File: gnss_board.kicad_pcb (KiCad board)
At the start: 4 copper layers, 102.2 x 100.3 mm, 118 parts, among them J1 Conn_01x10_Pin, J2 Serial Connector, J3 U.FL, J4 Conn_01x04_Pin, Q1 BC817, Q2 BC817, T1 LMUN2211LT1G, U1 H1102NL, U2 LAN8710A, U4 TX4138(ESOIC-8)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

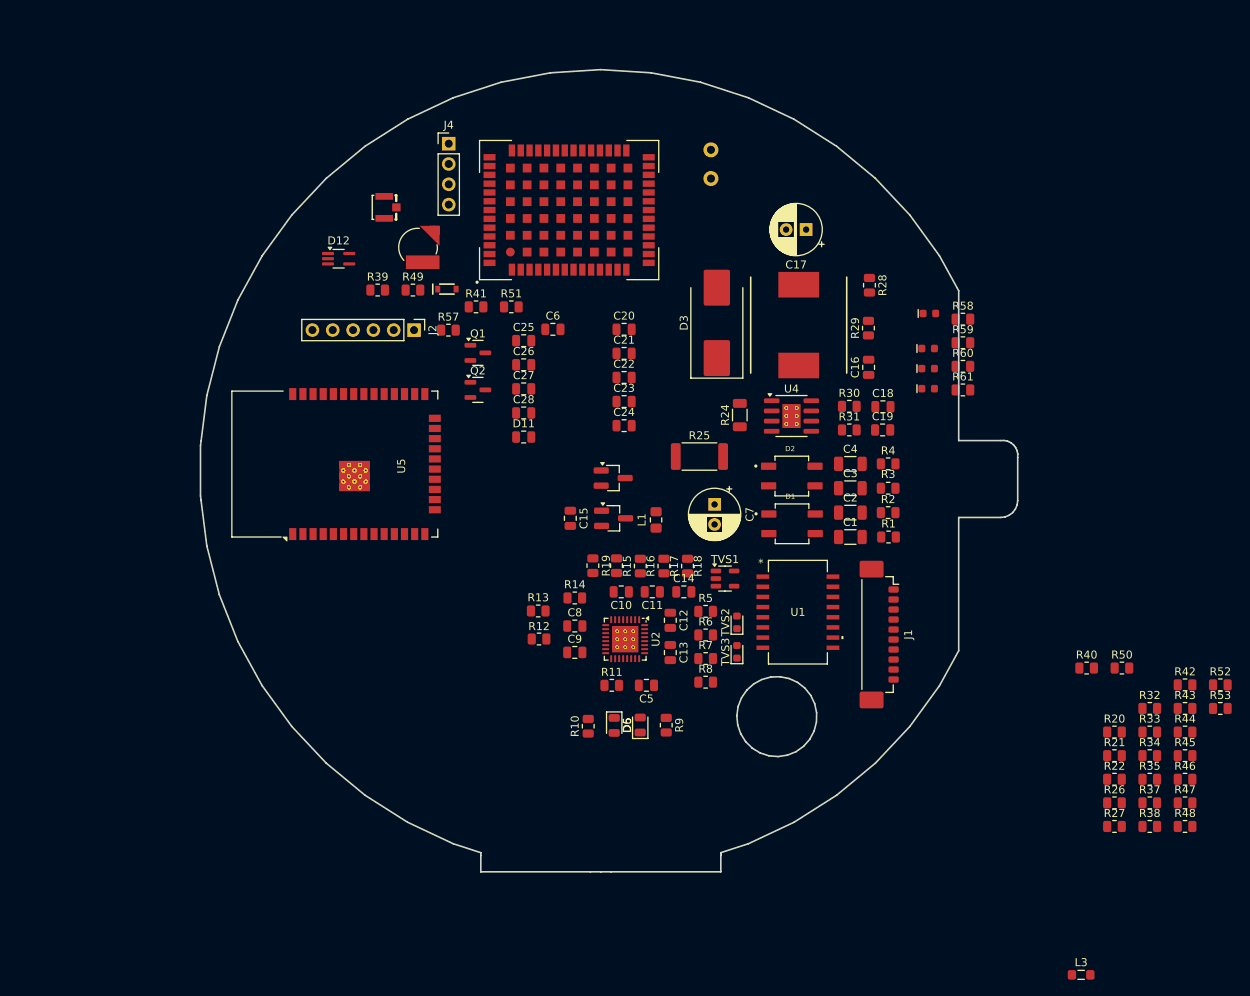
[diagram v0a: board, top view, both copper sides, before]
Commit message: All components have been added
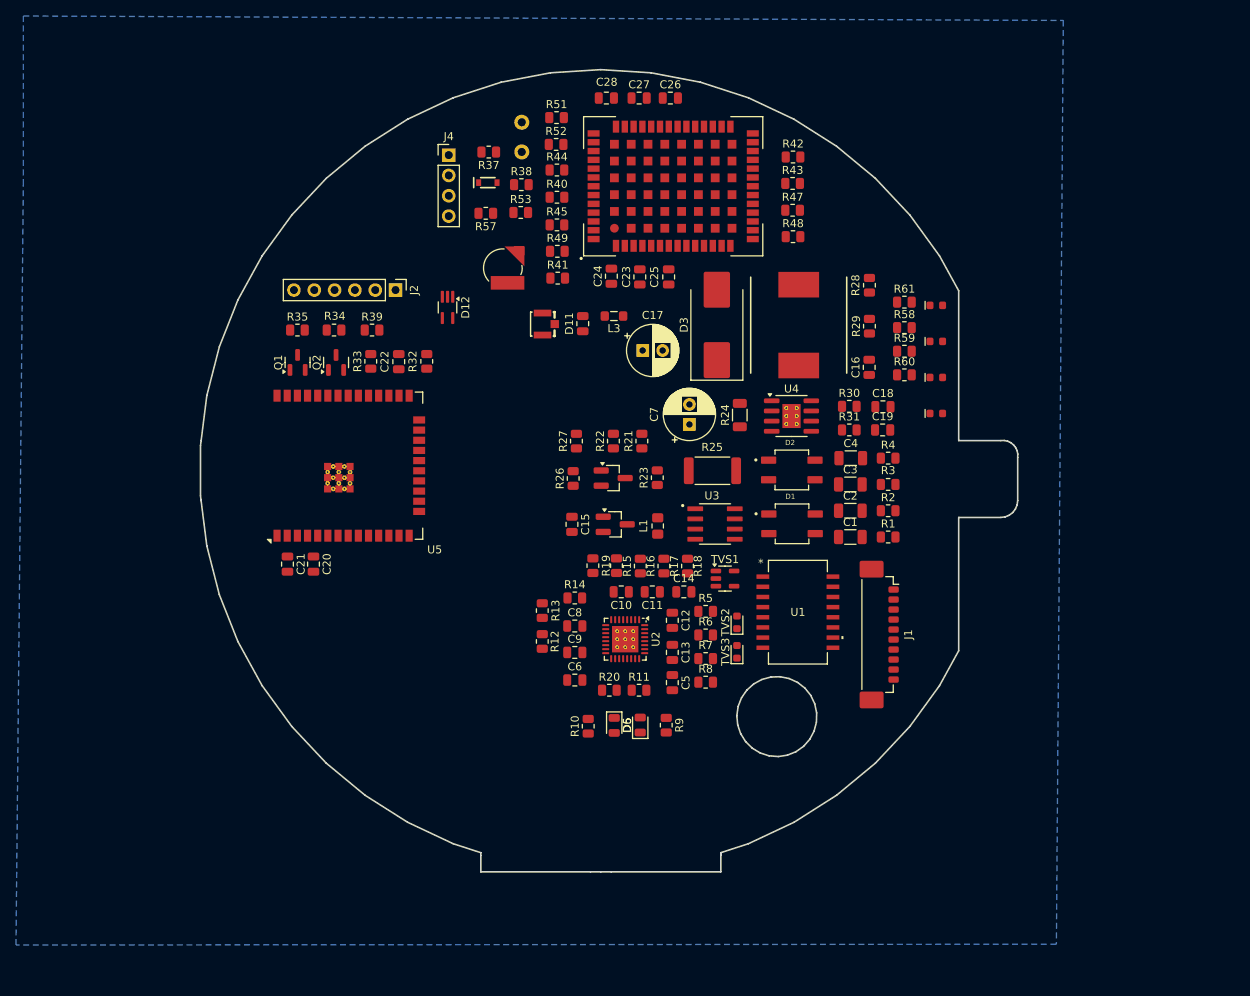
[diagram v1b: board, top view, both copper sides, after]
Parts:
- removed R46, R50: 33R, Resistor_SMD:R_0805_2012Metric
- added R23: 24.9K, Resistor_SMD:R_0805_2012Metric, F.Cu at (102.8, 79.5)
- added U3: TPS2375D, gnss_board:SOIC127P599X175-8N, F.Cu at (110.0, 85.2)
- U5: footprint RF_Module:ESP32-WROOM-32D -> RF_Module:ESP32-WROOM-32E
- moved R35 120.4 mm to (57.8, 61.0)
- moved R37 116.0 mm to (81.8, 38.8), turned to 180 degrees
- moved R34 115.0 mm to (62.4, 61.0), turned to 180 degrees
- moved R38 112.3 mm to (85.8, 42.8)
- moved R33 107.8 mm to (67.0, 64.9), turned to 90 degrees
- moved R53 107.2 mm to (85.8, 46.3)
- moved R52 107.0 mm to (90.2, 37.8)
- moved R44 105.4 mm to (90.3, 41.0)
- moved R45 102.8 mm to (90.3, 47.9)
- moved L3 101.0 mm to (97.4, 59.2), turned to 180 degrees
- moved R32 100.3 mm to (74.0, 64.9), turned to -90 degrees
- moved R47 88.8 mm to (119.7, 46.0)
- moved R40 88.6 mm to (90.3, 44.4)
- moved R48 88.5 mm to (119.8, 49.3)
- moved R27 82.7 mm to (92.7, 74.9), turned to 90 degrees
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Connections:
- U6 pad 21: Net-(U6-ERR_STAT) -> unconnected-(U6-ERR_STAT-Pad21)
- U6 pad 51: Net-(U6-EVENT) -> unconnected-(U6-EVENT-Pad51)
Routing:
- added copper zone on B.Cu, net GND

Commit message: Playing around with the auto-router
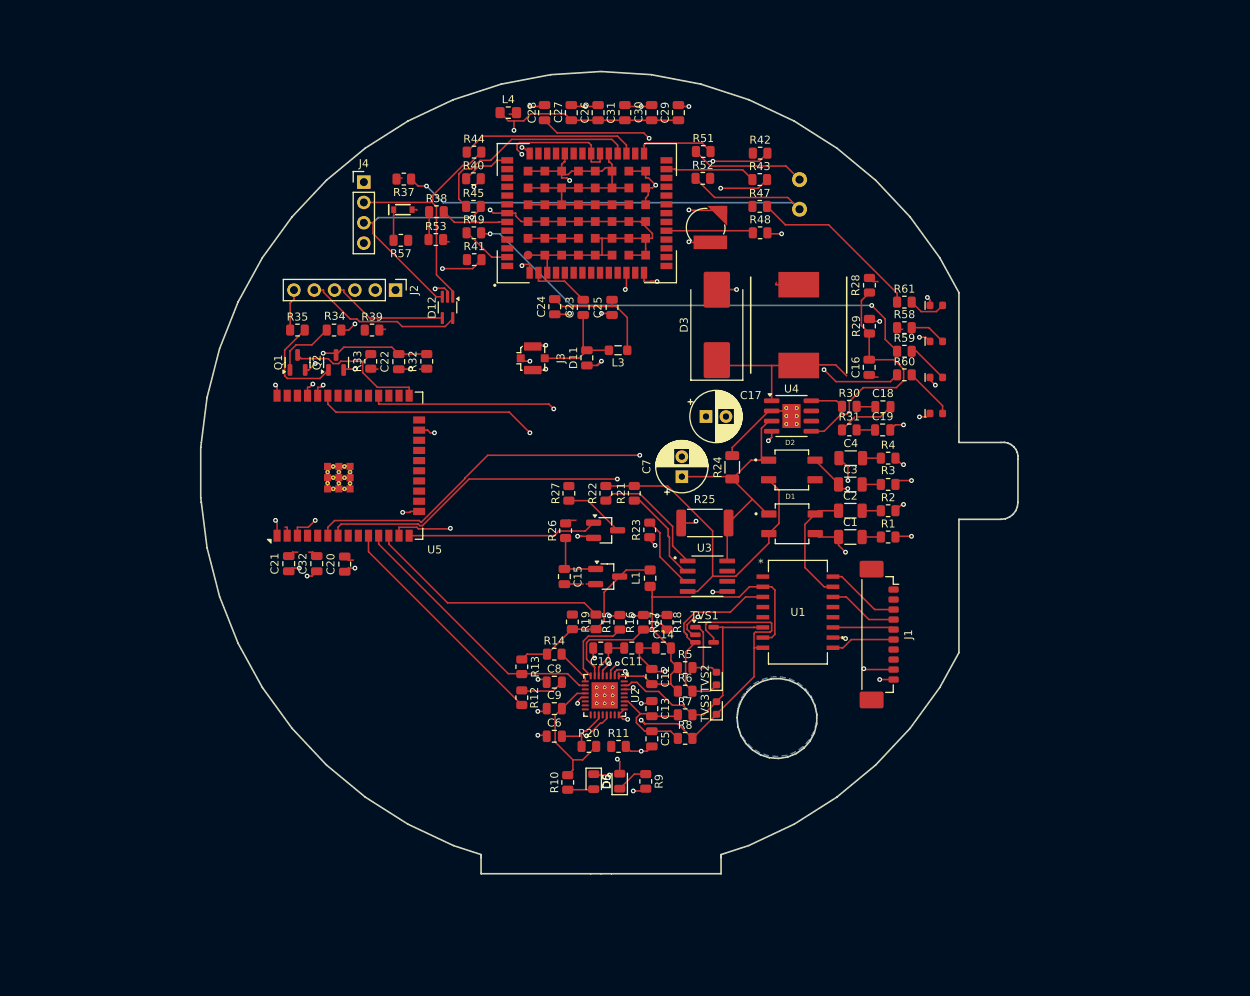
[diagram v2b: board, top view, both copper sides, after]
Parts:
- added C29: 10uF, Capacitor_SMD:C_0805_2012Metric, F.Cu at (105.5, 33.8)
- added C30: 10uF, Capacitor_SMD:C_0805_2012Metric, F.Cu at (102.1, 33.8)
- added C31: 10uF, Capacitor_SMD:C_0805_2012Metric, F.Cu at (98.8, 33.8)
- added C32: 22uF, Capacitor_SMD:C_0805_2012Metric, F.Cu at (60.2, 90.2)
- added L4: FB0805, Inductor_SMD:L_0805_2012Metric_Pad1.15x1.40mm_HandSolder, F.Cu at (84.2, 33.8)
- C26: value 2.2uF -> 10uF
- J3: footprint SparkFun-Connector:U.FL -> Connector_Coaxial:U.FL_Molex_MCRF_73412-0110_Vertical
- moved TP1 35.5 mm to (120.6, 45.9)
- moved TP2 35.5 mm to (120.6, 42.2)
- moved BT1 25.9 mm to (108.9, 48.2)
- moved R51 18.8 mm to (108.6, 38.7)
- moved R52 18.8 mm to (108.5, 42.0)
- moved C17 11.4 mm to (108.9, 71.8)
- moved U6 11.3 mm to (94.0, 46.4)
- moved J4 11.1 mm to (66.1, 42.5)
- moved R37 11.1 mm to (71.1, 42.1)
- moved R38 11.1 mm to (75.2, 46.2)
- moved R53 11.1 mm to (75.1, 49.7)
- moved R57 11.1 mm to (70.8, 49.8)
- moved D10 11.1 mm to (71.0, 45.9)
- moved R40 10.7 mm to (79.8, 42.1)
- moved R41 10.7 mm to (79.9, 52.2)
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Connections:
- net Net-(D3-K) renamed /SW
- C26 pad 2: +3.3V -> VCC
- C27 pad 2: +3.3V -> VCC
- U6 pad 33: +3.3V -> VCC
- U6 pad 34: +3.3V -> VCC
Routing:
- net GND: track 0.00 -> 223.9 mm, vias 0 -> 54
- net GNSS_RXD2: track 0.00 -> 94.8 mm, vias 0 -> 2
- net GNSS_TXD2: track 0.00 -> 91.7 mm, vias 0 -> 2
- net ETH_TX_EN: track 0.00 -> 72.5 mm, vias 0 -> 2
- net Net-(R37-Pad1): track 0.00 -> 64.7 mm, vias 0 -> 1
- net VDD1A: track 0.00 -> 60.3 mm
- net ETH_CLK_IN: track 0.00 -> 59.8 mm, vias 0 -> 2
- net GNSS_PPS: track 0.00 -> 59.6 mm, vias 0 -> 2
- net GNSS_TXD1: track 0.00 -> 53.2 mm, vias 0 -> 2
- net RD-: track 0.00 -> 47.3 mm, vias 0 -> 2
- net +3.3VLAN: track 0.00 -> 45.5 mm
- net VIN+: track 0.00 -> 44.3 mm, vias 0 -> 1
- net VCC: track 0.00 -> 43.2 mm, vias 0 -> 2
- net VIN-: track 0.00 -> 43.0 mm
- net +3.3V: track 0.00 -> 40.7 mm, vias 0 -> 17
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- added copper zone on In2.Cu, net +3.3V
- added copper zone on In1.Cu, net GND
